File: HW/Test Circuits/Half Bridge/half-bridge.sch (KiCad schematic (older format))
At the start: 11 parts, among them J1 CONTROL, J2 OUT, J3 PWR, J4 DT, P1 100K, Q1 IRL540, Q2 IRL540, U1 L6384E

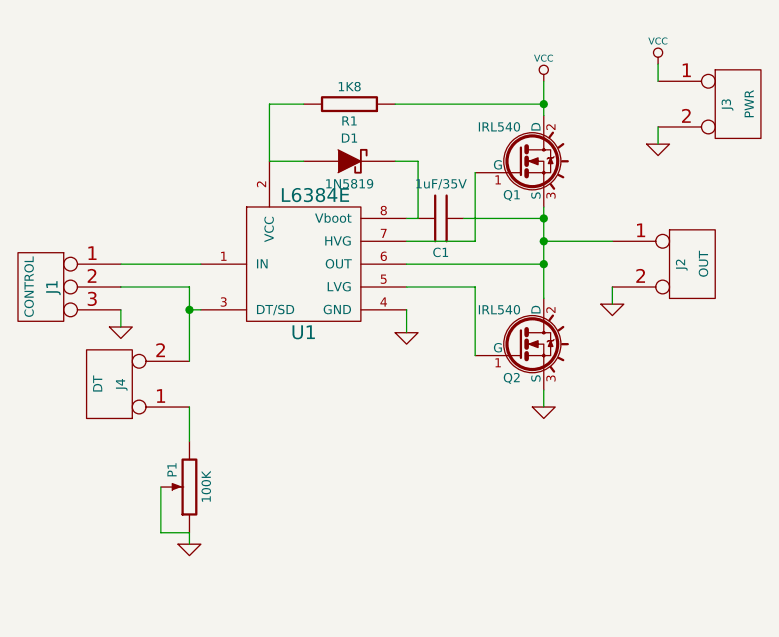
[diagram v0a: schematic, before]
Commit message: Hardware reorganization + cleanup MCUv2 renamed to Front Panel
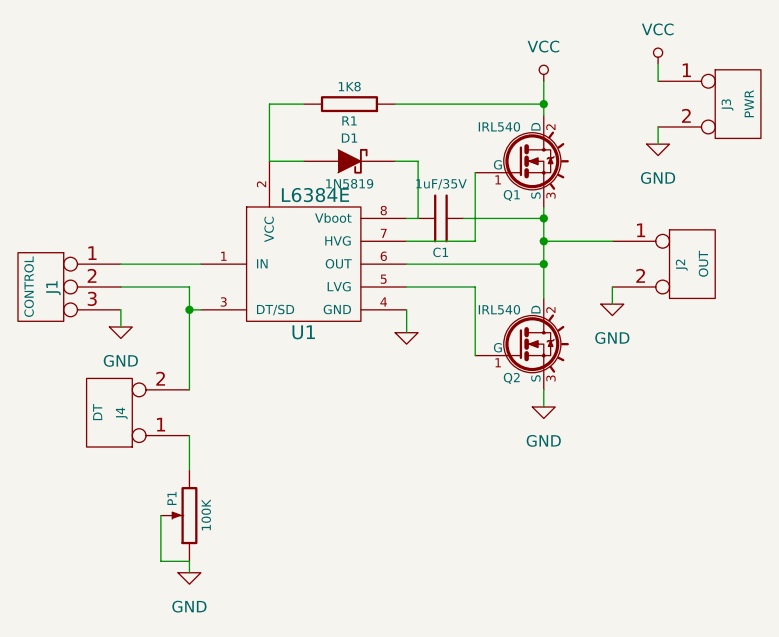
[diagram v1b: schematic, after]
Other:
- moved on the sheet: J4, P1
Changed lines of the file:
@@
 LIBS:memory
 LIBS:xilinx
-LIBS:special
 LIBS:microcontrollers
 LIBS:dsp
@@
 LIBS:contrib
 LIBS:valves
-EELAYER 27 0
+EELAYER 25 0
 EELAYER END
 $Descr A4 11693 8268
@@
 	6150 3000 6750 3000
 Wire Wire Line
-	6750 2750 6750 3150
+	6750 2750 6750 2800
+Wire Wire Line
+	6750 2800 6750 2900
+Wire Wire Line
+	6750 2900 6750 3000
+Wire Wire Line
+	6750 3000 6750 3150
 Connection ~ 6750 3000
 $Comp
@@
 	6100 2300 6750 2300
 Wire Wire Line
-	6750 2200 6750 2350
+	6750 2200 6750 2300
+Wire Wire Line
+	6750 2300 6750 2350
 $Comp
 L VCC #PWR01
 U 1 1 54A65829
 P 6750 2200
-F 0 "#PWR01" H 6750 2300 30  0001 C CNN
-F 1 "VCC" H 6750 2300 30  0000 C CNN
+F 0 "#PWR01" H 6750 2050 50  0001 C CNN
+F 1 "VCC" H 6750 2350 50  0000 C CNN
 F 2 "" H 6750 2200 60  0000 C CNN
 F 3 "" H 6750 2200 60  0000 C CNN
@@
 L VR P1
 U 1 1 54A6596A
-P 5200 3975
-F 0 "P1" H 5125 3900 40  0000 C CNN
-F 1 "100K" H 5200 4050 40  0000 C CNN
-F 2 "RV_BOU3296Y" H 5200 3975 60  0001 C CNN
-F 3 "~" H 5200 3975 60  0000 C CNN
-	1    5200 3975
+P 5200 4100
+F 0 "P1" H 5125 4025 40  0000 C CNN
+F 1 "100K" H 5200 4175 40  0000 C CNN
+F 2 "RV_BOU3296Y" H 5200 4100 60  0001 C CNN
+F 3 "~" H 5200 4100 60  0000 C CNN
+	1    5200 4100
 	0    1    1    0
 $EndComp
@@
 L GND #PWR03
 U 1 1 54A65979
-P 5200 4225
-F 0 "#PWR03" H 5200 4225 30  0001 C CNN
-F 1 "GND" H 5200 4155 30  0001 C CNN
-F 2 "" H 5200 4225 60  0000 C CNN
-F 3 "" H 5200 4225 60  0000 C CNN
-	1    5200 4225
+P 5200 4350
+F 0 "#PWR03" H 5200 4100 50  0001 C CNN
+F 1 "GND" H 5200 4200 50  0000 C CNN
+F 2 "" H 5200 4350 60  0000 C CNN
+F 3 "" H 5200 4350 60  0000 C CNN
+	1    5200 4350
 	1    0    0    -1
 $EndComp
@@
 	5250 3200 5200 3200
 Wire Wire Line
-	5200 3100 5200 3425
-Wire Wire Line
-	5075 3975 5075 4175
-Wire Wire Line
-	5075 4175 5200 4175
-Wire Wire Line
-	5200 4175 5200 4225
+	5200 3100 5200 3200
+Wire Wire Line
+	5200 3200 5200 3550
+Wire Wire Line
+	5075 4100 5075 4300
+Wire Wire Line
+	5075 4300 5200 4300
+Wire Wire Line
+	5200 4300 5200 4350
 $Comp
 L GND #PWR04
 U 1 1 54A65B18
 P 6750 3625
-F 0 "#PWR04" H 6750 3625 30  0001 C CNN
-F 1 "GND" H 6750 3555 30  0001 C CNN
+F 0 "#PWR04" H 6750 3375 50  0001 C CNN
+F 1 "GND" H 6750 3475 50  0000 C CNN
 F 2 "" H 6750 3625 60  0000 C CNN
 F 3 "" H 6750 3625 60  0000 C CNN
@@
 U 1 1 54A65C23
 P 4900 3275
-F 0 "#PWR05" H 4900 3275 30  0001 C CNN
-F 1 "GND" H 4900 3205 30  0001 C CNN
+F 0 "#PWR05" H 4900 3025 50  0001 C CNN
+F 1 "GND" H 4900 3125 50  0000 C CNN
 F 2 "" H 4900 3275 60  0000 C CNN
 F 3 "" H 4900 3275 60  0000 C CNN
@@
 U 1 1 54A65E50
 P 7050 3175
-F 0 "#PWR06" H 7050 3175 30  0001 C CNN
-F 1 "GND" H 7050 3105 30  0001 C CNN
+F 0 "#PWR06" H 7050 2925 50  0001 C CNN
+F 1 "GND" H 7050 3025 50  0000 C CNN
 F 2 "" H 7050 3175 60  0000 C CNN
 F 3 "" H 7050 3175 60  0000 C CNN
@@
 U 1 1 54A65ED7
 P 7250 2125
-F 0 "#PWR07" H 7250 2225 30  0001 C CNN
-F 1 "VCC" H 7250 2225 30  0000 C CNN
+F 0 "#PWR07" H 7250 1975 50  0001 C CNN
+F 1 "VCC" H 7250 2275 50  0000 C CNN
 F 2 "" H 7250 2125 60  0000 C CNN
 F 3 "" H 7250 2125 60  0000 C CNN
@@
 U 1 1 54A65EE6
 P 7250 2475
-F 0 "#PWR08" H 7250 2475 30  0001 C CNN
-F 1 "GND" H 7250 2405 30  0001 C CNN
+F 0 "#PWR08" H 7250 2225 50  0001 C CNN
+F 1 "GND" H 7250 2325 50  0000 C CNN
 F 2 "" H 7250 2475 60  0000 C CNN
 F 3 "" H 7250 2475 60  0000 C CNN
@@
 L CONN_2 J4
 U 1 1 54A7B78D
-P 4850 3525
-F 0 "J4" V 4800 3525 40  0000 C CNN
-F 1 "DT" V 4900 3525 40  0000 C CNN
-F 2 "HDR-2" H 4850 3525 60  0001 C CNN
-F 3 "" H 4850 3525 60  0000 C CNN
-	1    4850 3525
+P 4850 3650
+F 0 "J4" V 4800 3650 40  0000 C CNN
+F 1 "DT" V 4900 3650 40  0000 C CNN
+F 2 "HDR-2" H 4850 3650 60  0001 C CNN
+F 3 "" H 4850 3650 60  0000 C CNN
+	1    4850 3650
 	-1   0    0    1
 $EndComp
 Wire Wire Line
-	5200 3625 5200 3775
+	5200 3750 5200 3900
 $EndSCHEMATC
